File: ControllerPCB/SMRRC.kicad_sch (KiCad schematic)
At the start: 23 parts, among them J1 Conn_01x08_Socket, J2 Conn_01x05, J3 Conn_01x03, J4 Conn_02x06_Odd_Even, SW1 SW_Push, SW2 SW_Push, U1 THVD1500, U2 PIC16F15345-I/SO, U3 L78L05_SOT89

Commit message: Working on SM control
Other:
- note added: "+12V +12V GND GND Data + Data + Data - Data -"
- note added: "RS-485 RB4 nRE Receiver Enable RB5 RX1 RB6 DE Driver Enable RB7 TX1"
- note removed: "+12V +12V GND GND A A B B"

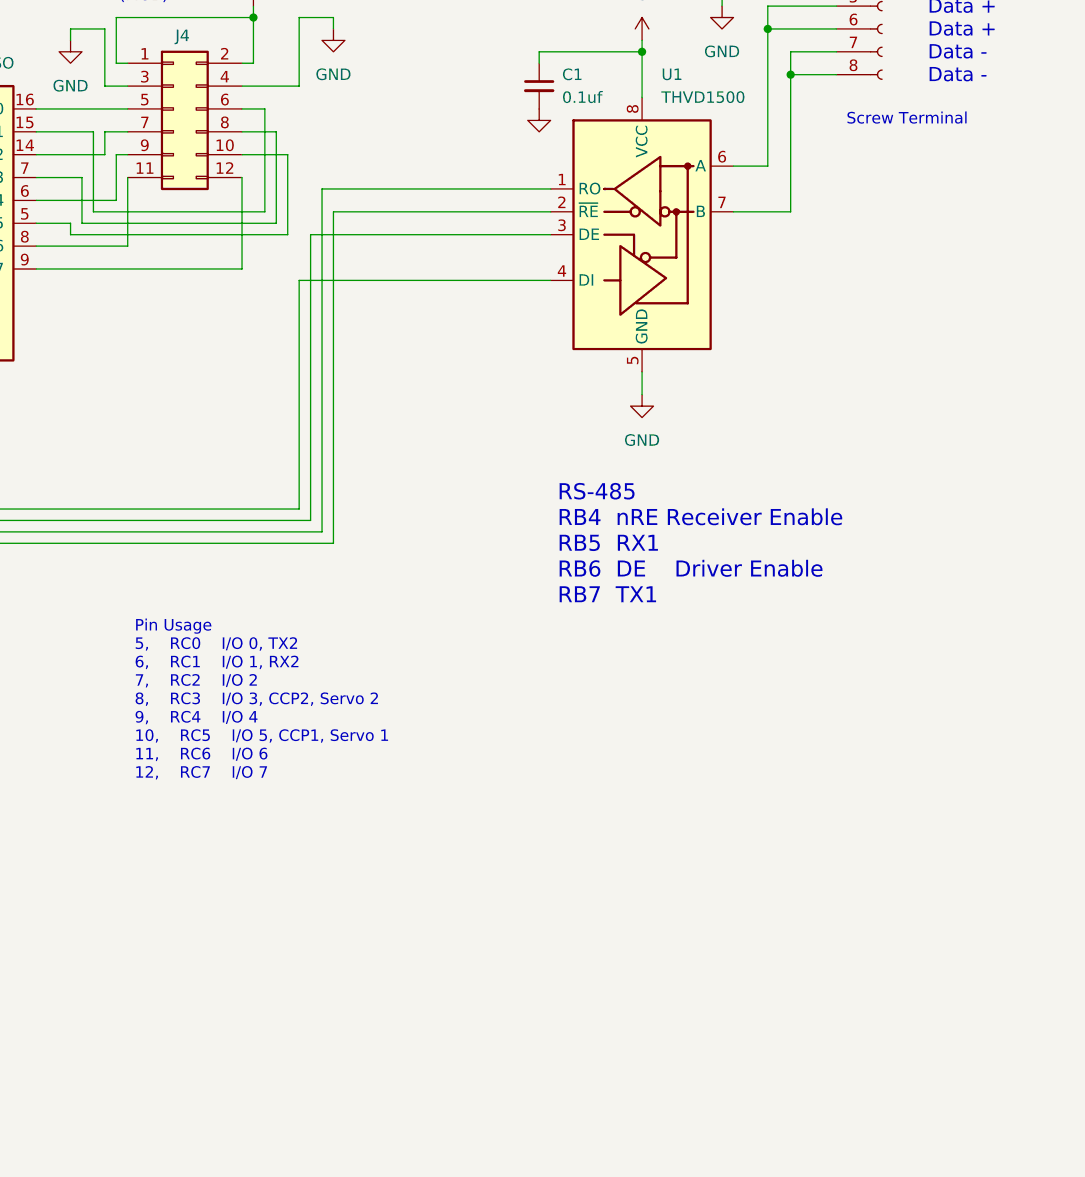
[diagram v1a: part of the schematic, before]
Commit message: Good test of USB to RS485
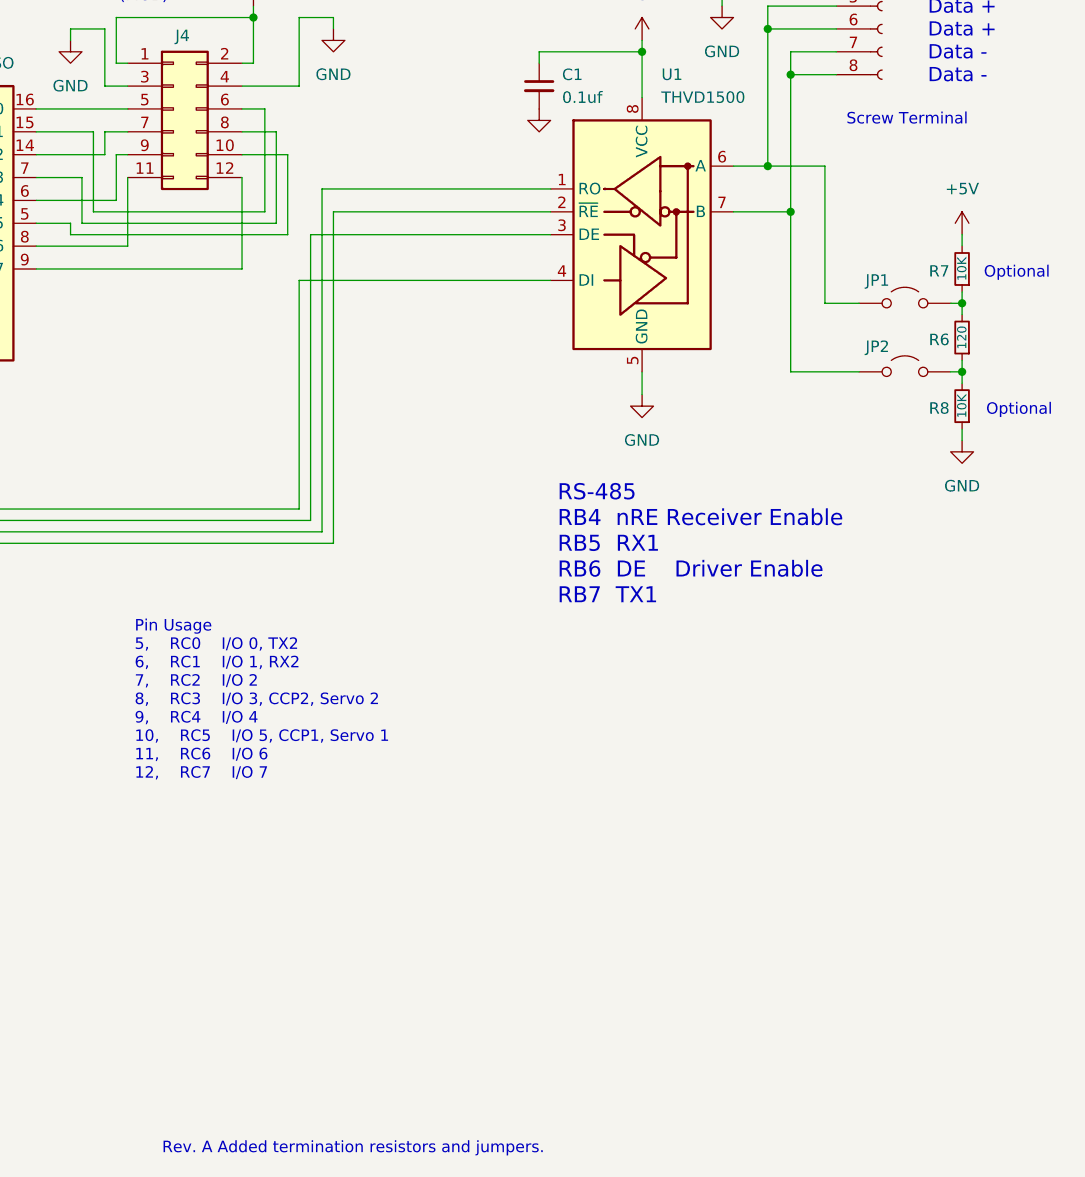
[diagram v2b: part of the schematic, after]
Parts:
- added JP1, JP2: Jumper_2_Open, Jumper:SolderJumper-2_P1.3mm_Open_RoundedPad1.0x1.5mm, symbol Jumper:Jumper_2_Open
- added R6: 120, Resistor_SMD:R_0805_2012Metric_Pad1.20x1.40mm_HandSolder, symbol Device:R_Small
- added R7, R8: 10K, Resistor_SMD:R_0805_2012Metric_Pad1.20x1.40mm_HandSolder, symbol Device:R_Small
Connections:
- net +5V: now also R7.2
- net GND: now also R8.1
- net at J1.5 (Pin_5), J1.6 (Pin_6), U1.6 (A): now also JP1.1 (A)
- net at J1.7 (Pin_7), J1.8 (Pin_8), U1.7 (B): now also JP2.1 (A)
- new net: JP2.2 (B), R6.1, R8.2
- new net: JP1.2 (B), R6.2, R7.1
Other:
- note added: "Optional"
- note added: "Rev. A Added termination resistors and jumpers."
